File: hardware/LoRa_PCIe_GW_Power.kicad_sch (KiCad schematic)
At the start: 46 parts, among them U201 3V3, U202 TPS62242DRV, U203 3V3, U204 STTS751, U205 NCP176BMX330TCG, U206 3V3

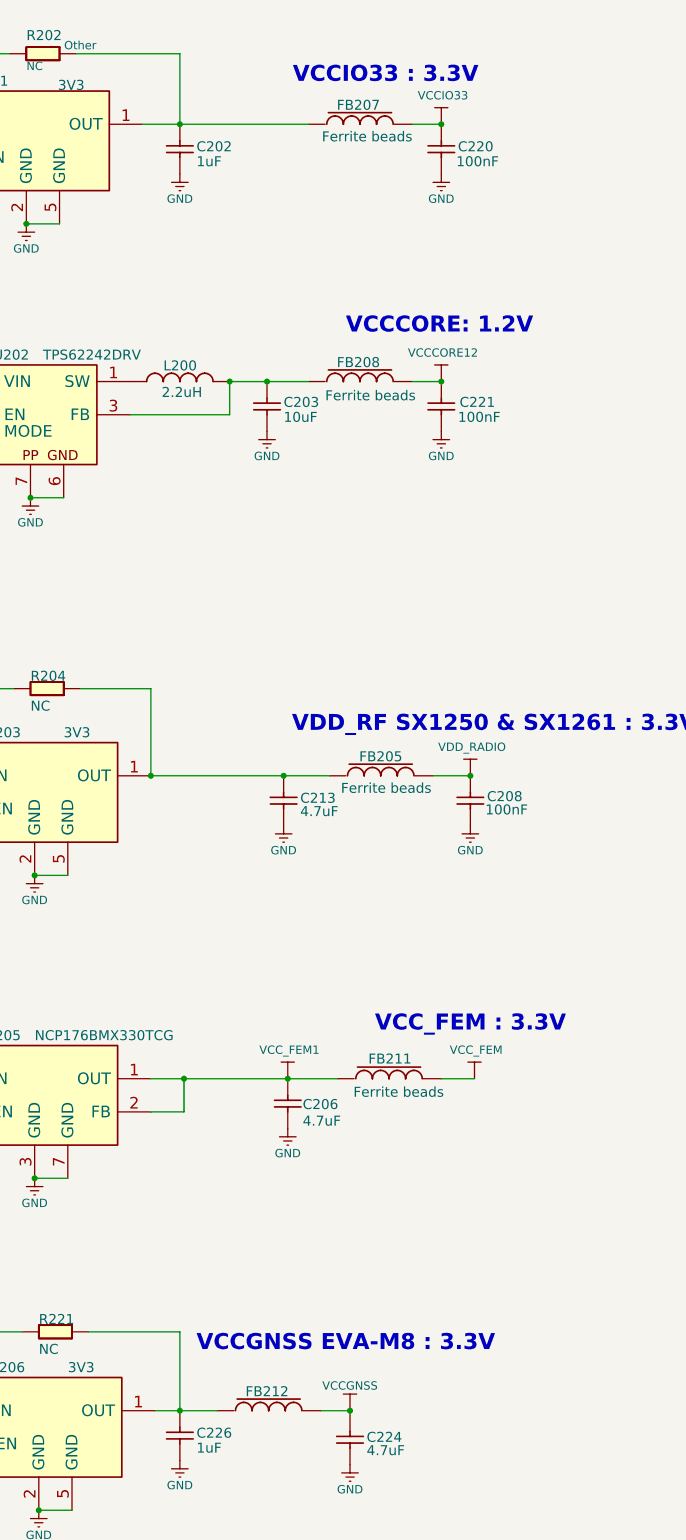
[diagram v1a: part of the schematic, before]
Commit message: Fixed ERC and Schematic to Layout parity errors.
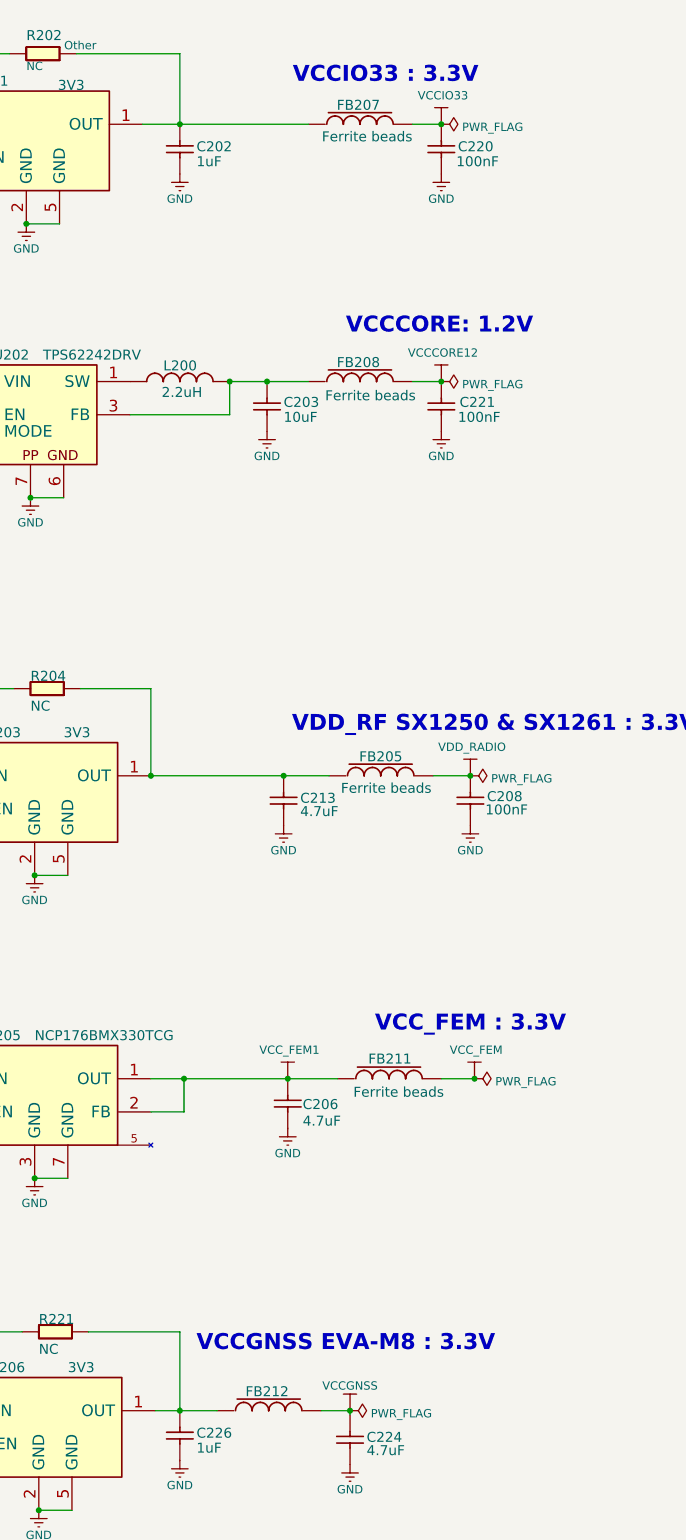
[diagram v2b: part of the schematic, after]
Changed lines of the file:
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@@
   (junction (at 33.02 151.13) (diameter 0) (color 0 0 0 0)
+  )
+  (junction (at 285.75 189.23) (diameter 0) (color 0 0 0 0)
   )
   (junction (at 196.215 240.03) (diameter 0) (color 0 0 0 0)
@@
     (pin "6")
     (pin "7")
-  )
-  (symbol (lib_id "LoRa_PCIe_GW-rescue:NCP114-") (at 210.82 153.035 0) (unit 1)
+    (pin "5")
+  )
+  (symbol (lib_name "NCP114-_1") (lib_id "LoRa_PCIe_GW-rescue:NCP114-") (at 210.82 153.035 0) (unit 1)
     (in_bom yes) (on_board yes)
     (property "Reference" "U203" (id 0) (at 210.82 137.16 0)
@@
     (pin "2")
   )
+  (symbol (lib_id "power:PWR_FLAG") (at 280.67 82.55 270) (unit 1)
+    (in_bom yes) (on_board yes) (fields_autoplaced)
+    (property "Reference" "#FLG0108" (id 0) (at 282.575 82.55 0)
+      (effects (font (size 1.27 1.27)) hide)
+    )
+    (property "Value" "PWR_FLAG" (id 1) (at 283.845 82.9838 90)
+      (effects (font (size 1.27 1.27)) (justify left))
+    )
+    (property "Footprint" "" (id 2) (at 280.67 82.55 0)
+      (effects (font (size 1.27 1.27)) hide)
+    )
+    (property "Datasheet" "~" (id 3) (at 280.67 82.55 0)
+      (effects (font (size 1.27 1.27)) hide)
+    )
+    (pin "1")
+  )
+  (symbol (lib_id "power:PWR_FLAG") (at 266.7 240.03 270) (unit 1)
+    (in_bom yes) (on_board yes) (fields_autoplaced)
+    (property "Reference" "#FLG0106" (id 0) (at 268.605 240.03 0)
+      (effects (font (size 1.27 1.27)) hide)
+    )
+    (property "Value" "PWR_FLAG" (id 1) (at 269.875 240.4638 90)
+      (effects (font (size 1.27 1.27)) (justify left))
+    )
+    (property "Footprint" "" (id 2) (at 266.7 240.03 0)
+      (effects (font (size 1.27 1.27)) hide)
+    )
+    (property "Datasheet" "~" (id 3) (at 266.7 240.03 0)
+      (effects (font (size 1.27 1.27)) hide)
+    )
+    (pin "1")
+  )
+  (symbol (lib_id "power:PWR_FLAG") (at 285.115 142.875 270) (unit 1)
+    (in_bom yes) (on_board yes) (fields_autoplaced)
+    (property "Reference" "#FLG0104" (id 0) (at 287.02 142.875 0)
+      (effects (font (size 1.27 1.27)) hide)
+    )
+    (property "Value" "PWR_FLAG" (id 1) (at 288.29 143.3088 90)
+      (effects (font (size 1.27 1.27)) (justify left))
+    )
+    (property "Footprint" "" (id 2) (at 285.115 142.875 0)
+      (effects (font (size 1.27 1.27)) hide)
+    )
+    (property "Datasheet" "~" (id 3) (at 285.115 142.875 0)
+      (effects (font (size 1.27 1.27)) hide)
+    )
+    (pin "1")
+  )
+  (symbol (lib_id "power:PWR_FLAG") (at 285.75 189.23 270) (unit 1)
+    (in_bom yes) (on_board yes) (fields_autoplaced)
+    (property "Reference" "#FLG0105" (id 0) (at 287.655 189.23 0)
+      (effects (font (size 1.27 1.27)) hide)
+    )
+    (property "Value" "PWR_FLAG" (id 1) (at 288.925 189.6638 90)
+      (effects (font (size 1.27 1.27)) (justify left))
+    )
+    (property "Footprint" "" (id 2) (at 285.75 189.23 0)
+      (effects (font (size 1.27 1.27)) hide)
+    )
+    (property "Datasheet" "~" (id 3) (at 285.75 189.23 0)
+      (effects (font (size 1.27 1.27)) hide)
+    )
+    (pin "1")
+  )
+  (symbol (lib_id "power:PWR_FLAG") (at 280.67 43.18 270) (unit 1)
+    (in_bom yes) (on_board yes) (fields_autoplaced)
+    (property "Reference" "#FLG0107" (id 0) (at 282.575 43.18 0)
+      (effects (font (size 1.27 1.27)) hide)
+    )
+    (property "Value" "PWR_FLAG" (id 1) (at 283.845 43.6138 90)
+      (effects (font (size 1.27 1.27)) (justify left))
+    )
+    (property "Footprint" "" (id 2) (at 280.67 43.18 0)
+      (effects (font (size 1.27 1.27)) hide)
+    )
+    (property "Datasheet" "~" (id 3) (at 280.67 43.18 0)
+      (effects (font (size 1.27 1.27)) hide)
+    )
+    (pin "1")
+  )
 )
